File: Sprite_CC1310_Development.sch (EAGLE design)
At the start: 67 parts, among them U1 NCP1402

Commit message: still working
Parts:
- added U$1: HDMID, HDMID:HDMID
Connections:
- net GND: now also U$1.19, U$1.FOOT1, U$1.FOOT2, U$1.FOOT3, U$1.FOOT4
- net SWO: now also U$1.15, U$1.16
- net TDI: now also U$1.13, U$1.14
- net VDDS: now also U$1.17, U$1.18
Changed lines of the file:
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@@
 <part name="C20" library="SparkFun" deviceset="CAP" device="0805" value="100 uF"/>
 <part name="GND34" library="SparkFun" deviceset="GND" device=""/>
+<part name="U$1" library="HDMID" deviceset="HDMID" device=""/>
+<part name="GND35" library="SparkFun" deviceset="GND" device=""/>
+<part name="GND36" library="SparkFun" deviceset="GND" device=""/>
 </parts>
 <sheets>
@@
 <instance part="C20" gate="G$1" x="180.34" y="15.24"/>
 <instance part="GND34" gate="1" x="180.34" y="10.16"/>
+<instance part="U$1" gate="G$1" x="195.58" y="149.86"/>
+<instance part="GND35" gate="1" x="175.26" y="175.26" rot="R180"/>
+<instance part="GND36" gate="1" x="167.64" y="137.16" rot="R270"/>
 </instances>
 <busses>
@@
 <pinref part="GND34" gate="1" pin="GND"/>
 </segment>
+<segment>
+<pinref part="U$1" gate="G$1" pin="FOOT4"/>
+<pinref part="U$1" gate="G$1" pin="FOOT3"/>
+<wire x1="208.28" y1="172.72" x2="200.66" y2="172.72" width="0.1524" layer="91"/>
+<pinref part="U$1" gate="G$1" pin="FOOT2"/>
+<wire x1="193.04" y1="172.72" x2="200.66" y2="172.72" width="0.1524" layer="91"/>
+<junction x="200.66" y="172.72"/>
+<pinref part="U$1" gate="G$1" pin="FOOT1"/>
+<wire x1="193.04" y1="172.72" x2="185.42" y2="172.72" width="0.1524" layer="91"/>
+<junction x="193.04" y="172.72"/>
+<pinref part="GND35" gate="1" pin="GND"/>
+<wire x1="175.26" y1="172.72" x2="185.42" y2="172.72" width="0.1524" layer="91"/>
+<junction x="185.42" y="172.72"/>
+</segment>
+<segment>
+<pinref part="U$1" gate="G$1" pin="19"/>
+<pinref part="GND36" gate="1" pin="GND"/>
+<wire x1="172.72" y1="144.78" x2="172.72" y2="137.16" width="0.1524" layer="91"/>
+<wire x1="172.72" y1="137.16" x2="170.18" y2="137.16" width="0.1524" layer="91"/>
+</segment>
 </net>
 <net name="RESET" class="0">
@@
 <junction x="193.04" y="20.32"/>
 </segment>
+<segment>
+<pinref part="U$1" gate="G$1" pin="17"/>
+<wire x1="177.8" y1="144.78" x2="177.8" y2="137.16" width="0.1524" layer="91"/>
+<label x="177.8" y="137.16" size="1.778" layer="95" rot="R90"/>
+</segment>
+<segment>
+<pinref part="U$1" gate="G$1" pin="18"/>
+<wire x1="175.26" y1="144.78" x2="175.26" y2="137.16" width="0.1524" layer="91"/>
+<label x="175.26" y="137.16" size="1.778" layer="95" rot="R90"/>
+</segment>
 </net>
 <net name="DCDC_SW" class="0">
@@
 <label x="124.46" y="45.72" size="1.778" layer="95"/>
 </segment>
+<segment>
+<pinref part="U$1" gate="G$1" pin="14"/>
+<wire x1="185.42" y1="144.78" x2="185.42" y2="137.16" width="0.1524" layer="91"/>
+<label x="185.42" y="137.16" size="1.778" layer="95" rot="R90"/>
+</segment>
+<segment>
+<pinref part="U$1" gate="G$1" pin="13"/>
+<wire x1="187.96" y1="144.78" x2="187.96" y2="137.16" width="0.1524" layer="91"/>
+<label x="187.96" y="137.16" size="1.778" layer="95" rot="R90"/>
+</segment>
 </net>
 <net name="SWO" class="0">
@@
 <label x="124.46" y="48.26" size="1.778" layer="95"/>
 </segment>
-</net>
+<segment>
+<pinref part="U$1" gate="G$1" pin="16"/>
+<wire x1="180.34" y1="144.78" x2="180.34" y2="137.16" width="0.1524" layer="91"/>
+<label x="180.34" y="137.16" size="1.778" layer="95" rot="R90"/>
+</segment>
+<segment>
+<pinref part="U$1" gate="G$1" pin="15"/>
+<wire x1="182.88" y1="144.78" x2="182.88" y2="137.16" width="0.1524" layer="91"/>
+<label x="182.88" y="137.16" size="1.778" layer="95" rot="R90"/>
+</segment>
+</net>

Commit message: still routing
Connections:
- net GND: now also MICROCONTROLLER.32
- net JTAG_TCKC: now also U$1.5, U$1.6
- net JTAG_TMSC: now also U$1.3, U$1.4
- net RESET: now also U$1.13, U$1.14
- net RXD: now also U$1.17, U$1.18
- net SWO: now also U$1.11, U$1.12; no longer U$1.15, U$1.16
- net TDI: now also U$1.10, U$1.9; no longer U$1.13, U$1.14
- net TDO: now also U$1.7, U$1.8
- net TXD: now also U$1.15, U$1.16
- net VDDS: now also U$1.1, U$1.2; no longer U$1.17, U$1.18
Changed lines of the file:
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@@
 <part name="GND35" library="SparkFun" deviceset="GND" device=""/>
 <part name="GND36" library="SparkFun" deviceset="GND" device=""/>
+<part name="GND37" library="SparkFun" deviceset="GND" device=""/>
 </parts>
 <sheets>
@@
 <instance part="GND35" gate="1" x="175.26" y="175.26" rot="R180"/>
 <instance part="GND36" gate="1" x="167.64" y="137.16" rot="R270"/>
+<instance part="GND37" gate="1" x="132.08" y="55.88"/>
 </instances>
 <busses>
@@
 <wire x1="172.72" y1="137.16" x2="170.18" y2="137.16" width="0.1524" layer="91"/>
 </segment>
+<segment>
+<pinref part="MICROCONTROLLER" gate="G$1" pin="32"/>
+<pinref part="GND37" gate="1" pin="GND"/>
+<wire x1="124.46" y1="58.42" x2="132.08" y2="58.42" width="0.1524" layer="91"/>
+</segment>
 </net>
 <net name="RESET" class="0">
@@
 <wire x1="152.4" y1="66.04" x2="162.56" y2="66.04" width="0.1524" layer="91"/>
 <junction x="152.4" y="66.04"/>
+</segment>
+<segment>
+<pinref part="U$1" gate="G$1" pin="14"/>
+<wire x1="185.42" y1="144.78" x2="185.42" y2="137.16" width="0.1524" layer="91"/>
+<label x="185.42" y="137.16" size="1.778" layer="95" rot="R90"/>
+</segment>
+<segment>
+<pinref part="U$1" gate="G$1" pin="13"/>
+<wire x1="187.96" y1="144.78" x2="187.96" y2="137.16" width="0.1524" layer="91"/>
+<label x="187.96" y="137.16" size="1.778" layer="95" rot="R90"/>
 </segment>
 </net>
@@
 </segment>
 <segment>
-<pinref part="U$1" gate="G$1" pin="17"/>
-<wire x1="177.8" y1="144.78" x2="177.8" y2="137.16" width="0.1524" layer="91"/>
-<label x="177.8" y="137.16" size="1.778" layer="95" rot="R90"/>
-</segment>
-<segment>
-<pinref part="U$1" gate="G$1" pin="18"/>
-<wire x1="175.26" y1="144.78" x2="175.26" y2="137.16" width="0.1524" layer="91"/>
-<label x="175.26" y="137.16" size="1.778" layer="95" rot="R90"/>
+<pinref part="U$1" gate="G$1" pin="2"/>
+<wire x1="215.9" y1="144.78" x2="215.9" y2="137.16" width="0.1524" layer="91"/>
+<label x="215.9" y="137.16" size="1.778" layer="95" rot="R90"/>
+</segment>
+<segment>
+<pinref part="U$1" gate="G$1" pin="1"/>
+<wire x1="218.44" y1="144.78" x2="218.44" y2="137.16" width="0.1524" layer="91"/>
+<label x="218.44" y="137.16" size="1.778" layer="95" rot="R90"/>
 </segment>
 </net>
@@
 <label x="63.5" y="40.64" size="1.778" layer="95"/>
 </segment>
+<segment>
+<pinref part="U$1" gate="G$1" pin="4"/>
+<wire x1="210.82" y1="144.78" x2="210.82" y2="137.16" width="0.1524" layer="91"/>
+<label x="210.82" y="132.08" size="1.778" layer="95" rot="R90"/>
+</segment>
+<segment>
+<pinref part="U$1" gate="G$1" pin="3"/>
+<wire x1="213.36" y1="144.78" x2="213.36" y2="137.16" width="0.1524" layer="91"/>
+<label x="213.36" y="132.08" size="1.778" layer="95" rot="R90"/>
+</segment>
 </net>
 <net name="JTAG_TCKC" class="0">
@@
 <wire x1="124.46" y1="40.64" x2="137.16" y2="40.64" width="0.1524" layer="91"/>
 <label x="124.46" y="40.64" size="1.778" layer="95"/>
+</segment>
+<segment>
+<pinref part="U$1" gate="G$1" pin="6"/>
+<wire x1="205.74" y1="144.78" x2="205.74" y2="137.16" width="0.1524" layer="91"/>
+<label x="205.74" y="132.08" size="1.778" layer="95" rot="R90"/>
+</segment>
+<segment>
+<pinref part="U$1" gate="G$1" pin="5"/>
+<wire x1="208.28" y1="144.78" x2="208.28" y2="137.16" width="0.1524" layer="91"/>
+<label x="208.28" y="132.08" size="1.778" layer="95" rot="R90"/>
 </segment>
 </net>
@@
 <label x="337.82" y="218.44" size="1.778" layer="95"/>
 </segment>
+<segment>
+<pinref part="U$1" gate="G$1" pin="18"/>
+<wire x1="175.26" y1="144.78" x2="175.26" y2="137.16" width="0.1524" layer="91"/>
+<label x="175.26" y="137.16" size="1.778" layer="95" rot="R90"/>
+</segment>
+<segment>
+<pinref part="U$1" gate="G$1" pin="17"/>
+<wire x1="177.8" y1="144.78" x2="177.8" y2="137.16" width="0.1524" layer="91"/>
+<label x="177.8" y="137.16" size="1.778" layer="95" rot="R90"/>
+</segment>
 </net>
 <net name="TXD" class="0">
@@
 <wire x1="353.06" y1="223.52" x2="363.22" y2="223.52" width="0.1524" layer="91"/>
 <label x="358.14" y="223.52" size="1.778" layer="95"/>
+</segment>
+<segment>
+<pinref part="U$1" gate="G$1" pin="16"/>
+<wire x1="180.34" y1="144.78" x2="180.34" y2="137.16" width="0.1524" layer="91"/>
+<label x="180.34" y="137.16" size="1.778" layer="95" rot="R90"/>
+</segment>
+<segment>
+<pinref part="U$1" gate="G$1" pin="15"/>
+<wire x1="182.88" y1="144.78" x2="182.88" y2="137.16" width="0.1524" layer="91"/>
+<label x="182.88" y="137.16" size="1.778" layer="95" rot="R90"/>
 </segment>
 </net>
@@
 <label x="124.46" y="43.18" size="1.778" layer="95"/>
 </segment>
+<segment>
+<pinref part="U$1" gate="G$1" pin="8"/>
+<wire x1="200.66" y1="144.78" x2="200.66" y2="137.16" width="0.1524" layer="91"/>
+<label x="200.66" y="137.16" size="1.778" layer="95" rot="R90"/>
+</segment>
+<segment>
+<pinref part="U$1" gate="G$1" pin="7"/>
+<wire x1="203.2" y1="144.78" x2="203.2" y2="137.16" width="0.1524" layer="91"/>
+<label x="203.2" y="137.16" size="1.778" layer="95" rot="R90"/>
+</segment>
 </net>
 <net name="TDI" class="0">
@@
 </segment>
 <segment>
-<pinref part="U$1" gate="G$1" pin="14"/>
-<wire x1="185.42" y1="144.78" x2="185.42" y2="137.16" width="0.1524" layer="91"/>
-<label x="185.42" y="137.16" size="1.778" layer="95" rot="R90"/>
-</segment>
-<segment>
-<pinref part="U$1" gate="G$1" pin="13"/>
-<wire x1="187.96" y1="144.78" x2="187.96" y2="137.16" width="0.1524" layer="91"/>
-<label x="187.96" y="137.16" size="1.778" layer="95" rot="R90"/>
+<pinref part="U$1" gate="G$1" pin="10"/>
+<wire x1="195.58" y1="144.78" x2="195.58" y2="137.16" width="0.1524" layer="91"/>
+<label x="195.58" y="137.16" size="1.778" layer="95" rot="R90"/>
+</segment>
+<segment>
+<pinref part="U$1" gate="G$1" pin="9"/>
+<wire x1="198.12" y1="144.78" x2="198.12" y2="137.16" width="0.1524" layer="91"/>
+<label x="198.12" y="137.16" size="1.778" layer="95" rot="R90"/>
 </segment>
 </net>
@@
 </segment>
 <segment>
-<pinref part="U$1" gate="G$1" pin="16"/>
-<wire x1="180.34" y1="144.78" x2="180.34" y2="137.16" width="0.1524" layer="91"/>
-<label x="180.34" y="137.16" size="1.778" layer="95" rot="R90"/>
-</segment>
-<segment>
-<pinref part="U$1" gate="G$1" pin="15"/>
-<wire x1="182.88" y1="144.78" x2="182.88" y2="137.16" width="0.1524" layer="91"/>
-<label x="182.88" y="137.16" size="1.778" layer="95" rot="R90"/>
-</segment>
-</net>
+<pinref part="U$1" gate="G$1" pin="12"/>
+<wire x1="190.5" y1="144.78" x2="190.5" y2="137.16" width="0.1524" layer="91"/>
+<label x="190.5" y="137.16" size="1.778" layer="95" rot="R90"/>
+</segment>
+<segment>
+<pinref part="U$1" gate="G$1" pin="11"/>
+<wire x1="193.04" y1="144.78" x2="193.04" y2="137.16" width="0.1524" layer="91"/>
+<label x="193.04" y="137.16" size="1.778" layer="95" rot="R90"/>
+</segment>
+</net>

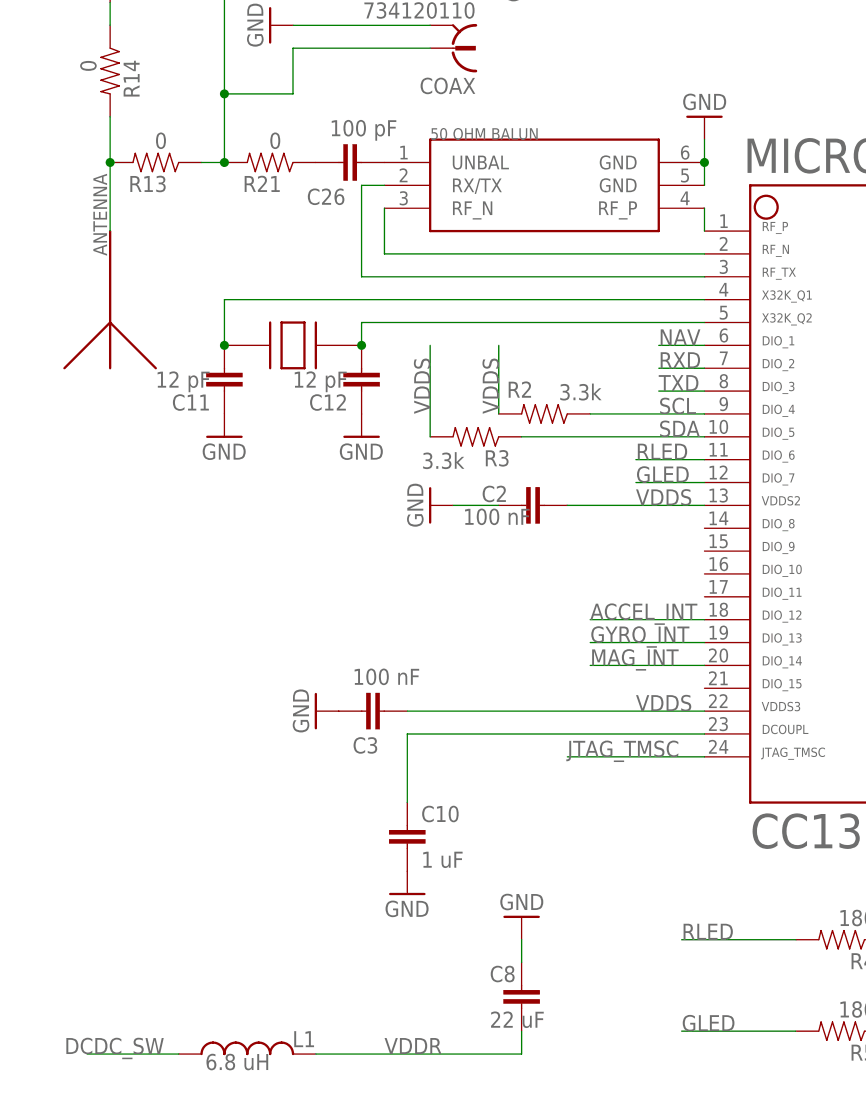
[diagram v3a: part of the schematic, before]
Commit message: fixed antenna
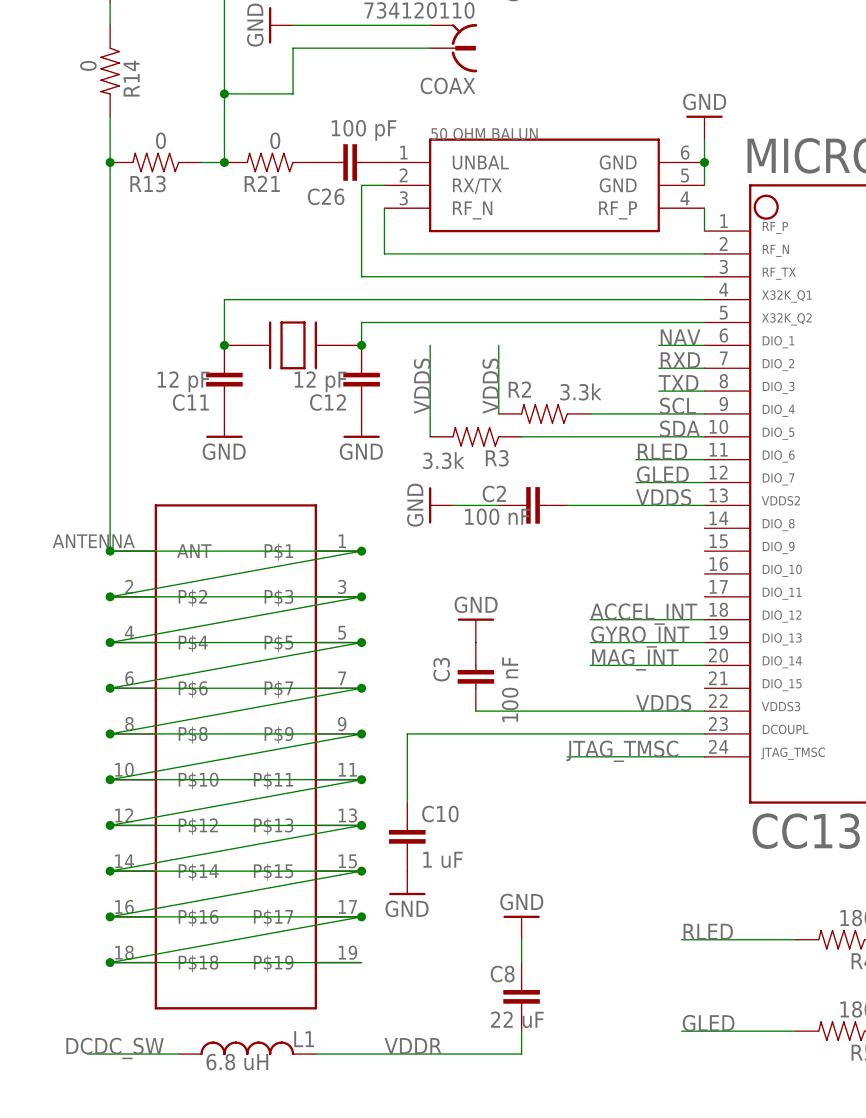
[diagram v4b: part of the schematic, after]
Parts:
- removed U$3: 915_MHZ_PCB_ANTENNA, 915_MHZ_PCB_ANTENNA:915_MHZ_PCB_ANTENNA
- added U$6: PCB_ANTENNA, PCB_ANTENNA:PCB_ANTENNA
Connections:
- removed net N$10: R13.2, R14.2, U$3.ANTENNA
- new net ANTENNA: R13.2, R14.2, U$6.ANT, U$6.P$1, U$6.P$10, U$6.P$11, U$6.P$12, U$6.P$13, U$6.P$14, U$6.P$15, U$6.P$16, U$6.P$17, U$6.P$18, U$6.P$19, U$6.P$2, U$6.P$3, U$6.P$4, U$6.P$5, U$6.P$6, U$6.P$7, U$6.P$8, U$6.P$9
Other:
- moved on the sheet: C3
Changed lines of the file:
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@@
 <layers>
 <layer number="1" name="Top" color="4" fill="1" visible="no" active="no"/>
+<layer number="2" name="Route2" color="1" fill="3" visible="no" active="no"/>
+<layer number="15" name="Route15" color="4" fill="6" visible="no" active="no"/>
 <layer number="16" name="Bottom" color="1" fill="1" visible="no" active="no"/>
 <layer number="17" name="Pads" color="2" fill="1" visible="no" active="no"/>
@@
 <layer number="59" name="tCarbon" color="7" fill="1" visible="no" active="no"/>
 <layer number="60" name="bCarbon" color="7" fill="1" visible="no" active="no"/>
+<layer number="88" name="SimResults" color="9" fill="1" visible="yes" active="yes"/>
+<layer number="89" name="SimProbes" color="9" fill="1" visible="yes" active="yes"/>
 <layer number="90" name="Modules" color="5" fill="1" visible="yes" active="yes"/>
 <layer number="91" name="Nets" color="2" fill="1" visible="yes" active="yes"/>
@@
 <part name="R19" library="SparkFun" deviceset="RESISTOR" device="0402-RES" value="3.3k"/>
 <part name="R20" library="SparkFun" deviceset="RESISTOR" device="0402-RES" value="331"/>
-<part name="U$3" library="915_MHZ_PCB_ANTENNA" deviceset="915_MHZ_PCB_ANTENNA" device=""/>
 <part name="BALUN" library="JOHANSON_BALUN" deviceset="JOHANSON_BALUN" device=""/>
 <part name="GND44" library="SparkFun" deviceset="GND" device=""/>
@@
 <part name="GND36" library="SparkFun" deviceset="GND" device=""/>
 <part name="GND37" library="SparkFun" deviceset="GND" device=""/>
+<part name="U$6" library="PCB_ANTENNA" deviceset="PCB_ANTENNA" device=""/>
 </parts>
 <sheets>
@@
 </instance>
 <instance part="GND3" gate="1" x="48.26" y="68.58" rot="R270"/>
-<instance part="C3" gate="G$1" x="40.64" y="45.72" smashed="yes" rot="R270">
-<attribute name="NAME" x="39.624" y="41.021" size="1.778" layer="95"/>
-<attribute name="VALUE" x="39.624" y="48.641" size="1.778" layer="96"/>
-</instance>
-<instance part="GND4" gate="1" x="35.56" y="45.72" rot="R270"/>
+<instance part="C3" gate="G$1" x="53.34" y="50.8" smashed="yes" rot="R180">
+<attribute name="NAME" x="48.641" y="51.816" size="1.778" layer="95" rot="R270"/>
+<attribute name="VALUE" x="56.261" y="51.816" size="1.778" layer="96" rot="R270"/>
+</instance>
+<instance part="GND4" gate="1" x="53.34" y="55.88" rot="R180"/>
 <instance part="C4" gate="G$1" x="142.24" y="88.9" smashed="yes" rot="R90">
 <attribute name="NAME" x="145.796" y="88.519" size="1.778" layer="95" rot="R180"/>
@@
 </instance>
 <instance part="R20" gate="G$1" x="200.66" y="238.76"/>
-<instance part="U$3" gate="G$1" x="12.7" y="99.06" smashed="yes" rot="R180"/>
 <instance part="BALUN" gate="G$1" x="60.96" y="104.14" smashed="yes"/>
 <instance part="GND44" gate="1" x="78.74" y="111.76" rot="R180"/>
@@
 <instance part="GND36" gate="1" x="167.64" y="137.16" rot="R270"/>
 <instance part="GND37" gate="1" x="132.08" y="55.88"/>
+<instance part="U$6" gate="G$1" x="27.94" y="40.64" smashed="yes" rot="R270"/>
 </instances>
 <busses>
@@
 <pinref part="C3" gate="G$1" pin="1"/>
 <pinref part="MICROCONTROLLER" gate="G$1" pin="22"/>
-<wire x1="45.72" y1="45.72" x2="78.74" y2="45.72" width="0.1524" layer="91"/>
+<wire x1="53.34" y1="45.72" x2="78.74" y2="45.72" width="0.1524" layer="91"/>
 <label x="71.12" y="45.72" size="1.778" layer="95"/>
 </segment>
@@
 </segment>
 </net>
-<net name="N$10" class="0">
-<segment>
-<pinref part="R13" gate="G$1" pin="2"/>
-<pinref part="R14" gate="G$1" pin="2"/>
-<wire x1="12.7" y1="106.68" x2="12.7" y2="111.76" width="0.1524" layer="91"/>
-<pinref part="U$3" gate="G$1" pin="ANTENNA"/>
-<wire x1="12.7" y1="99.06" x2="12.7" y2="106.68" width="0.1524" layer="91"/>
-<junction x="12.7" y="106.68"/>
-</segment>
-</net>
 <net name="N$14" class="0">
 <segment>
@@
 </segment>
 </net>
+<net name="ANTENNA" class="0">
+<segment>
+<pinref part="U$6" gate="G$1" pin="ANT"/>
+<pinref part="U$6" gate="G$1" pin="P$1"/>
+<wire x1="12.7" y1="63.5" x2="40.64" y2="63.5" width="0.1524" layer="91"/>
+<pinref part="U$6" gate="G$1" pin="P$2"/>
+<wire x1="40.64" y1="63.5" x2="12.7" y2="58.42" width="0.1524" layer="91"/>
+<junction x="40.64" y="63.5"/>
+<pinref part="U$6" gate="G$1" pin="P$3"/>
+<wire x1="12.7" y1="58.42" x2="40.64" y2="58.42" width="0.1524" layer="91"/>
+<junction x="12.7" y="58.42"/>
+<pinref part="U$6" gate="G$1" pin="P$4"/>
+<wire x1="40.64" y1="58.42" x2="12.7" y2="53.34" width="0.1524" layer="91"/>
+<junction x="40.64" y="58.42"/>
+<pinref part="U$6" gate="G$1" pin="P$5"/>
+<wire x1="12.7" y1="53.34" x2="40.64" y2="53.34" width="0.1524" layer="91"/>
+<junction x="12.7" y="53.34"/>
+<pinref part="U$6" gate="G$1" pin="P$6"/>
+<wire x1="40.64" y1="53.34" x2="12.7" y2="48.26" width="0.1524" layer="91"/>
+<junction x="40.64" y="53.34"/>
+<pinref part="U$6" gate="G$1" pin="P$7"/>
+<wire x1="12.7" y1="48.26" x2="40.64" y2="48.26" width="0.1524" layer="91"/>
+<junction x="12.7" y="48.26"/>
+<pinref part="U$6" gate="G$1" pin="P$8"/>
+<wire x1="40.64" y1="48.26" x2="12.7" y2="43.18" width="0.1524" layer="91"/>
+<junction x="40.64" y="48.26"/>
+<pinref part="U$6" gate="G$1" pin="P$9"/>
+<wire x1="12.7" y1="43.18" x2="40.64" y2="43.18" width="0.1524" layer="91"/>
+<junction x="12.7" y="43.18"/>
+<pinref part="U$6" gate="G$1" pin="P$10"/>
+<wire x1="40.64" y1="43.18" x2="12.7" y2="38.1" width="0.1524" layer="91"/>
+<junction x="40.64" y="43.18"/>
+<pinref part="U$6" gate="G$1" pin="P$11"/>
+<wire x1="12.7" y1="38.1" x2="40.64" y2="38.1" width="0.1524" layer="91"/>
+<junction x="12.7" y="38.1"/>
+<pinref part="U$6" gate="G$1" pin="P$12"/>
+<wire x1="40.64" y1="38.1" x2="12.7" y2="33.02" width="0.1524" layer="91"/>
+<junction x="40.64" y="38.1"/>
+<pinref part="U$6" gate="G$1" pin="P$13"/>
+<wire x1="12.7" y1="33.02" x2="40.64" y2="33.02" width="0.1524" layer="91"/>
+<junction x="12.7" y="33.02"/>
+<pinref part="U$6" gate="G$1" pin="P$14"/>
+<wire x1="40.64" y1="33.02" x2="12.7" y2="27.94" width="0.1524" layer="91"/>
+<junction x="40.64" y="33.02"/>
+<pinref part="U$6" gate="G$1" pin="P$15"/>
+<wire x1="12.7" y1="27.94" x2="40.64" y2="27.94" width="0.1524" layer="91"/>
+<junction x="12.7" y="27.94"/>
+<pinref part="U$6" gate="G$1" pin="P$16"/>
+<wire x1="40.64" y1="27.94" x2="12.7" y2="22.86" width="0.1524" layer="91"/>
+<junction x="40.64" y="27.94"/>
+<pinref part="U$6" gate="G$1" pin="P$17"/>
+<wire x1="12.7" y1="22.86" x2="40.64" y2="22.86" width="0.1524" layer="91"/>
+<junction x="12.7" y="22.86"/>
+<pinref part="U$6" gate="G$1" pin="P$18"/>
+<wire x1="40.64" y1="22.86" x2="12.7" y2="17.78" width="0.1524" layer="91"/>
+<junction x="40.64" y="22.86"/>
+<pinref part="U$6" gate="G$1" pin="P$19"/>
+<wire x1="12.7" y1="17.78" x2="40.64" y2="17.78" width="0.1524" layer="91"/>
+<junction x="12.7" y="17.78"/>
+<pinref part="R13" gate="G$1" pin="2"/>
+<pinref part="R14" gate="G$1" pin="2"/>
+<wire x1="12.7" y1="106.68" x2="12.7" y2="111.76" width="0.1524" layer="91"/>
+<wire x1="12.7" y1="63.5" x2="12.7" y2="106.68" width="0.1524" layer="91"/>
+<junction x="12.7" y="63.5"/>
+<junction x="12.7" y="106.68"/>
+</segment>
+</net>
